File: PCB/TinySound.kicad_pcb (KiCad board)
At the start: 4 copper layers, 15.2 x 15.7 mm, 20 parts, among them J1 Conn_01x02, J2 Conn_01x02, J3 Micro_SD_Card_Det, J4 Conn_01x04, J5 Conn_01x02, U1 MAX98360AENL+, U2 STM32G030KxT, U3 MAX98360xxxB+

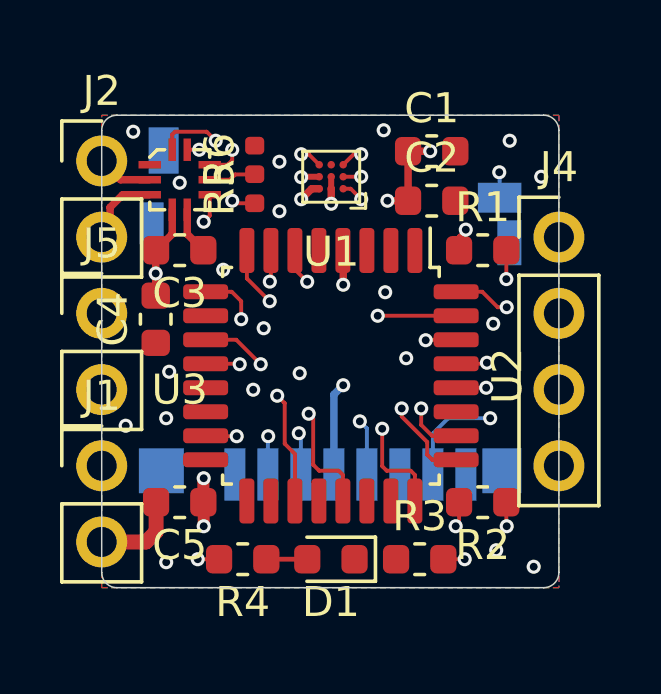
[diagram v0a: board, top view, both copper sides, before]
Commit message: [PCB] Additional resistors for SD card
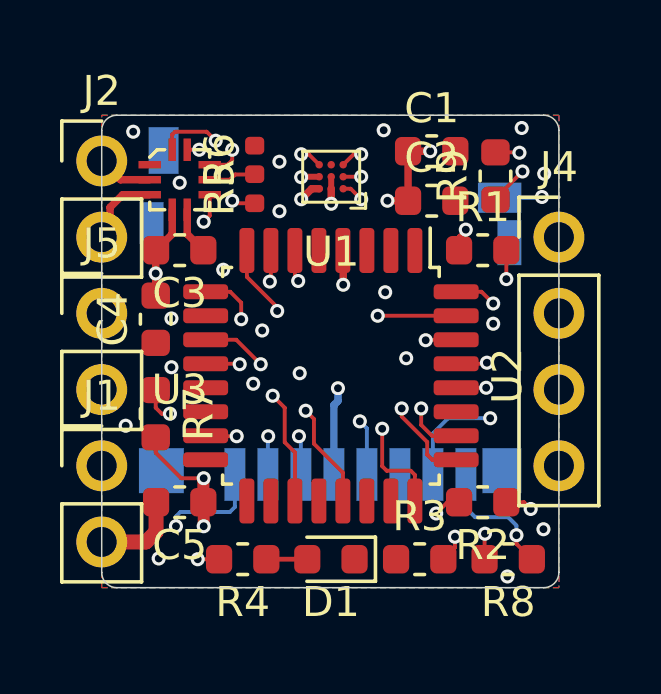
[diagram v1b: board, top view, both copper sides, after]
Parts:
- added R7: 10k, Resistor_SMD:R_0603_1608Metric, F.Cu at (101.8, 110.0)
- added R8: 10k, Resistor_SMD:R_0603_1608Metric, F.Cu at (113.5, 114.8)
- added R9: 10k, Resistor_SMD:R_0603_1608Metric, F.Cu at (113.1, 102.0)
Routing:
- net +3V3: track 61.9 -> 72.7 mm, vias 11 -> 13
- net /SD_MISO: track 9.49 -> 18.7 mm, vias 2 -> 3
- net Net-(J3-Pad1): track 0.00 -> 8.48 mm, vias 0 -> 2
- net Net-(J3-Pad8): track 0.00 -> 4.38 mm, vias 0 -> 1
- net /BOOT0_WAKEUP: track 22.3 -> 20.6 mm
- net /AU_BCLK: track 16.8 -> 17.7 mm

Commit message: [PCB] Fixed wiring error for SWD
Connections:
- net /BOOT0_WAKEUP renamed /SWCLK_BOOT0_WAKEUP
- net /SWCLK renamed /GPIO
- J4 pad 2: /SWDIO -> /NRST
- J4 pad 3: /NRST -> /SWDIO
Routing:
- net /SWDIO: track 12.5 -> 9.97 mm
- net /NRST: track 16.0 -> 18.3 mm

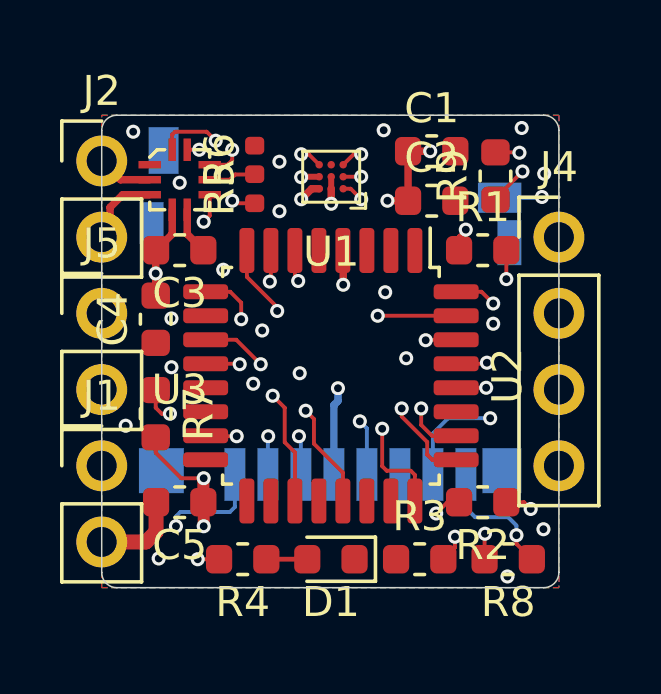
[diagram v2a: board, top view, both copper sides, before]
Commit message: [PCB] Moved resistor and redid the necessary routing!
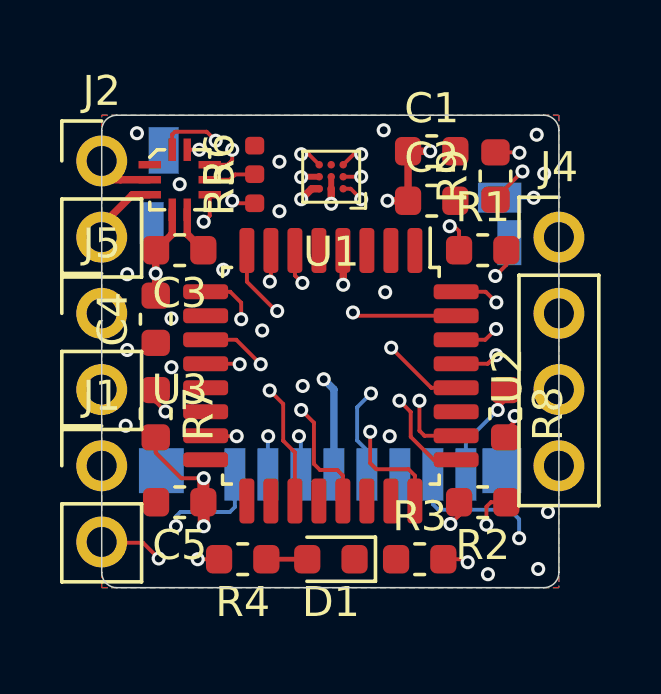
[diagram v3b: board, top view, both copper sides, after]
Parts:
- moved R8 4.85 mm to (113.5, 110.0), turned to 270 degrees
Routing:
- net /NRST: track 18.3 -> 28.6 mm
- net /SD_CLK: track 13.3 -> 9.12 mm
- net /SD_MISO: track 18.7 -> 22.2 mm
- net /SWCLK_BOOT0_WAKEUP: track 20.6 -> 22.7 mm
- net /GPIO: track 12.0 -> 10.6 mm
- net Net-(J2-Pad2): track 10.7 -> 9.63 mm
- net Net-(J3-Pad8): track 4.38 -> 3.36 mm
- net GND: track 4.23 -> 3.28 mm, vias 20 -> 21
- net +3V3: track 72.7 -> 73.5 mm
- net /SD_MOSI: track 9.29 -> 9.97 mm

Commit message: [PCB] Minor tweaks
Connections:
- J4 pad 2: /NRST -> /SWDIO
- J4 pad 3: /SWDIO -> /SWCLK_BOOT0_WAKEUP
- J4 pad 4: /SWCLK_BOOT0_WAKEUP -> /NRST
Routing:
- net /NRST: track 28.6 -> 17.2 mm
- net /SWDIO: track 9.93 -> 11.6 mm
- net /SWCLK_BOOT0_WAKEUP: track 22.7 -> 24.1 mm
- net /AU_BCLK: track 17.7 -> 16.3 mm
- net +3V3: track 73.5 -> 74.1 mm

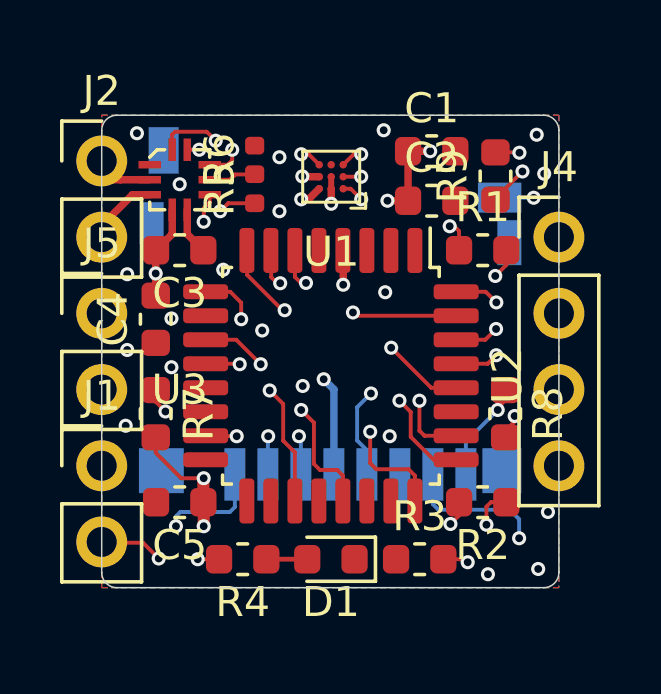
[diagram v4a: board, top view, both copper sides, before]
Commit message: [PCB] Some adjustments to solder mask for Gerber export
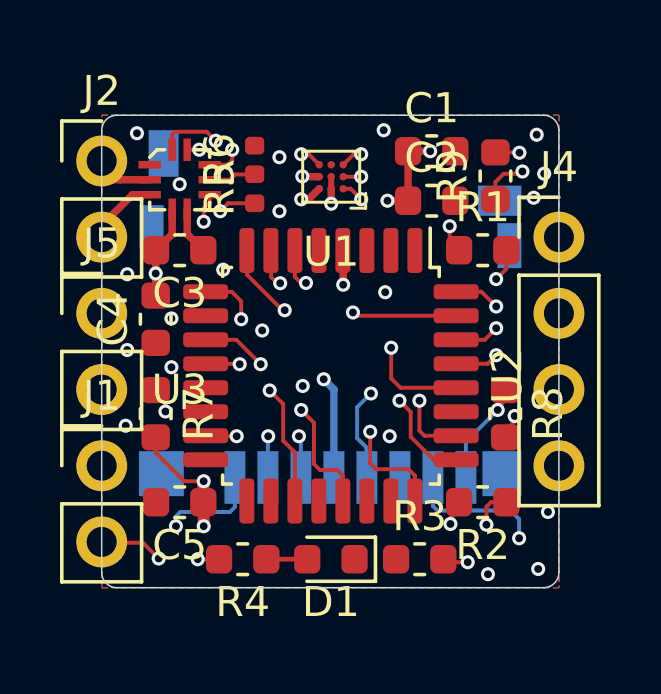
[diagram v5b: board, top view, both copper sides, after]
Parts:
- moved J3 0.10 mm to (107.6, 111.2)
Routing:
- net /SD_CLK: track 9.12 -> 10.0 mm
- net /SD_MISO: track 22.2 -> 22.8 mm
- net /SD_CS: track 17.3 -> 17.8 mm

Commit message: [PCB] Generated interactive HTML BOM
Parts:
- U1: footprint Package_BGA:Maxim_WLP-9_1.595x1.415_Layout3x3_P0.4mm_Ball0.27mm_Pad0.25mm_NSMD -> TinySound:Maxim_WLP-9_1.595x1.415_Layout3x3_P0.4mm_Ball0.27mm_Pad0.25mm_NSMD
